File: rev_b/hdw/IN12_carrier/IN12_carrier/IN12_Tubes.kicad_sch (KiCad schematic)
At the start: 14 parts

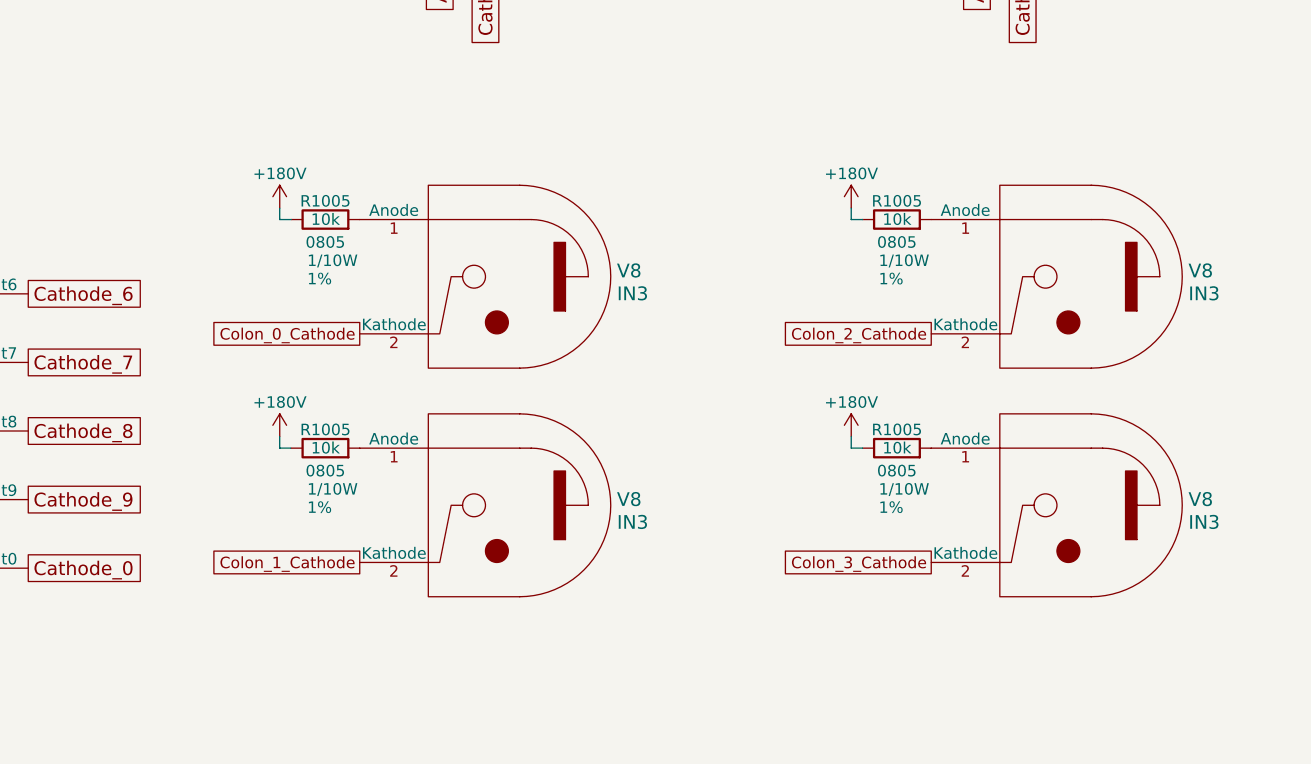
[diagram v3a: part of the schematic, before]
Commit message: added BOM for IN12 carrier, finished routing, some schematic tweaks, adjusted design rules for ERC
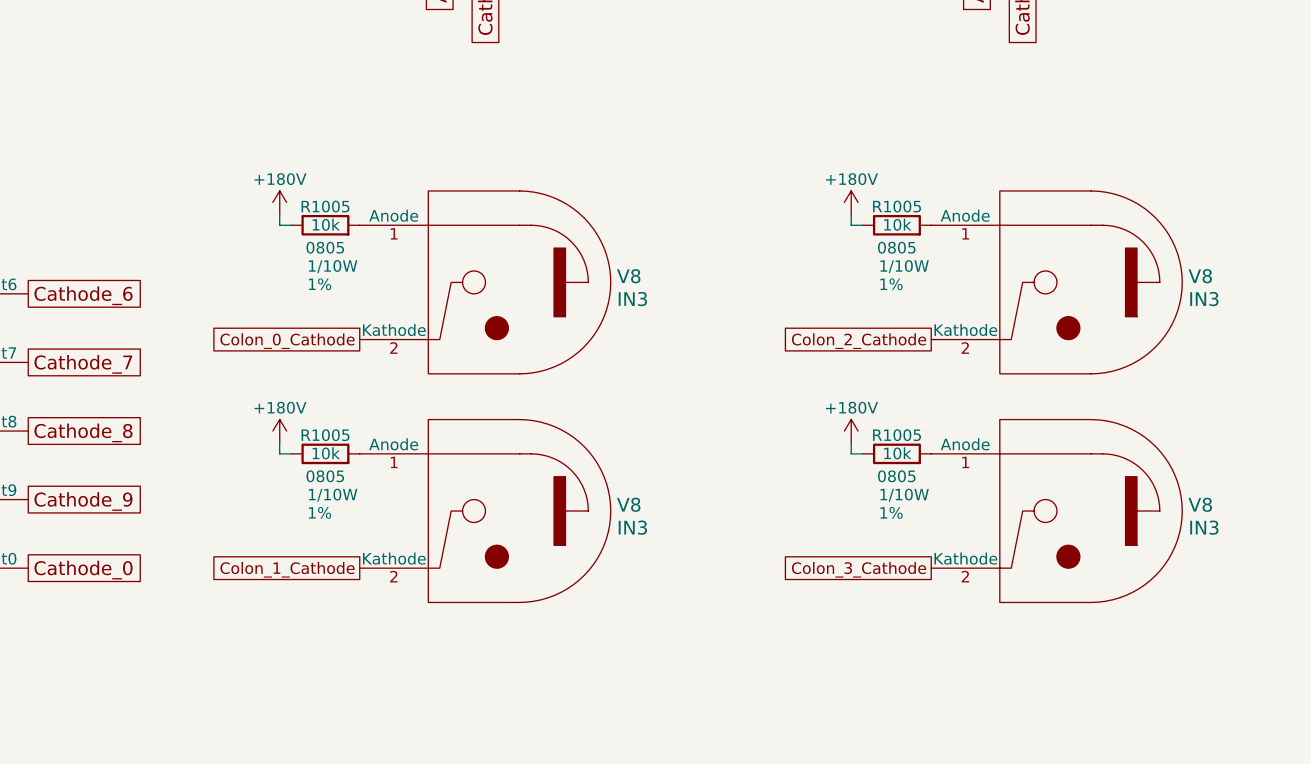
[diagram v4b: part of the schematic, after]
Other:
- moved on the sheet: R1005, V8

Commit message: assigned digikey pns to IN12 carrier board parts
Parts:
- R1005: Digi-Key PN (none) -> 541-3015-1-ND
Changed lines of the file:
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@@
       (effects (font (size 1.27 1.27)))
+    )
+    (property "Digi-Key PN" "541-3015-1-ND" (at 162.56 127 0)
+      (effects (font (size 1.27 1.27)) hide)
     )
     (pin "1")
@@
       (effects (font (size 1.27 1.27)))
     )
+    (property "Digi-Key PN" "541-3015-1-ND" (at 162.56 152.4 0)
+      (effects (font (size 1.27 1.27)) hide)
+    )
     (pin "1")
     (pin "2")
@@
     (property "display_footprint" "0805" (at 226.06 129.54 90)
       (effects (font (size 1.27 1.27)))
+    )
+    (property "Digi-Key PN" "541-3015-1-ND" (at 226.06 127 0)
+      (effects (font (size 1.27 1.27)) hide)
     )
     (pin "1")
@@
       (effects (font (size 1.27 1.27)))
     )
-    (pin "1")
+    (property "Digi-Key PN" "541-3015-1-ND" (at 226.06 152.4 0)
+      (effects (font (size 1.27 1.27)) hide)
+    )
+    (pin "1")
